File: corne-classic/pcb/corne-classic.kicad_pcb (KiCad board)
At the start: 2 copper layers, 133.8 x 92.2 mm, 98 parts, among them J1 MJ-4PP-9, J2 OLED, J3 LED, P1 i2c-pin, P2 i2c-pin, SW1 SW_PUSH, SW10 SW_PUSH, SW11 SW_PUSH, SW12 SW_PUSH, SW13 SW_PUSH, SW14 SW_PUSH, SW15 SW_PUSH, SW16 SW_PUSH, SW17 SW_PUSH, SW18 SW_PUSH, SW19 SW_PUSH, SW2 SW_PUSH, SW20 SW_PUSH, SW21 SW_PUSH, SW3 SW_PUSH, SW4 SW_PUSH, SW5 SW_PUSH, SW6 SW_PUSH, SW7 SW_PUSH, SW8 SW_PUSH, SW9 SW_PUSH, U1 ProMicro

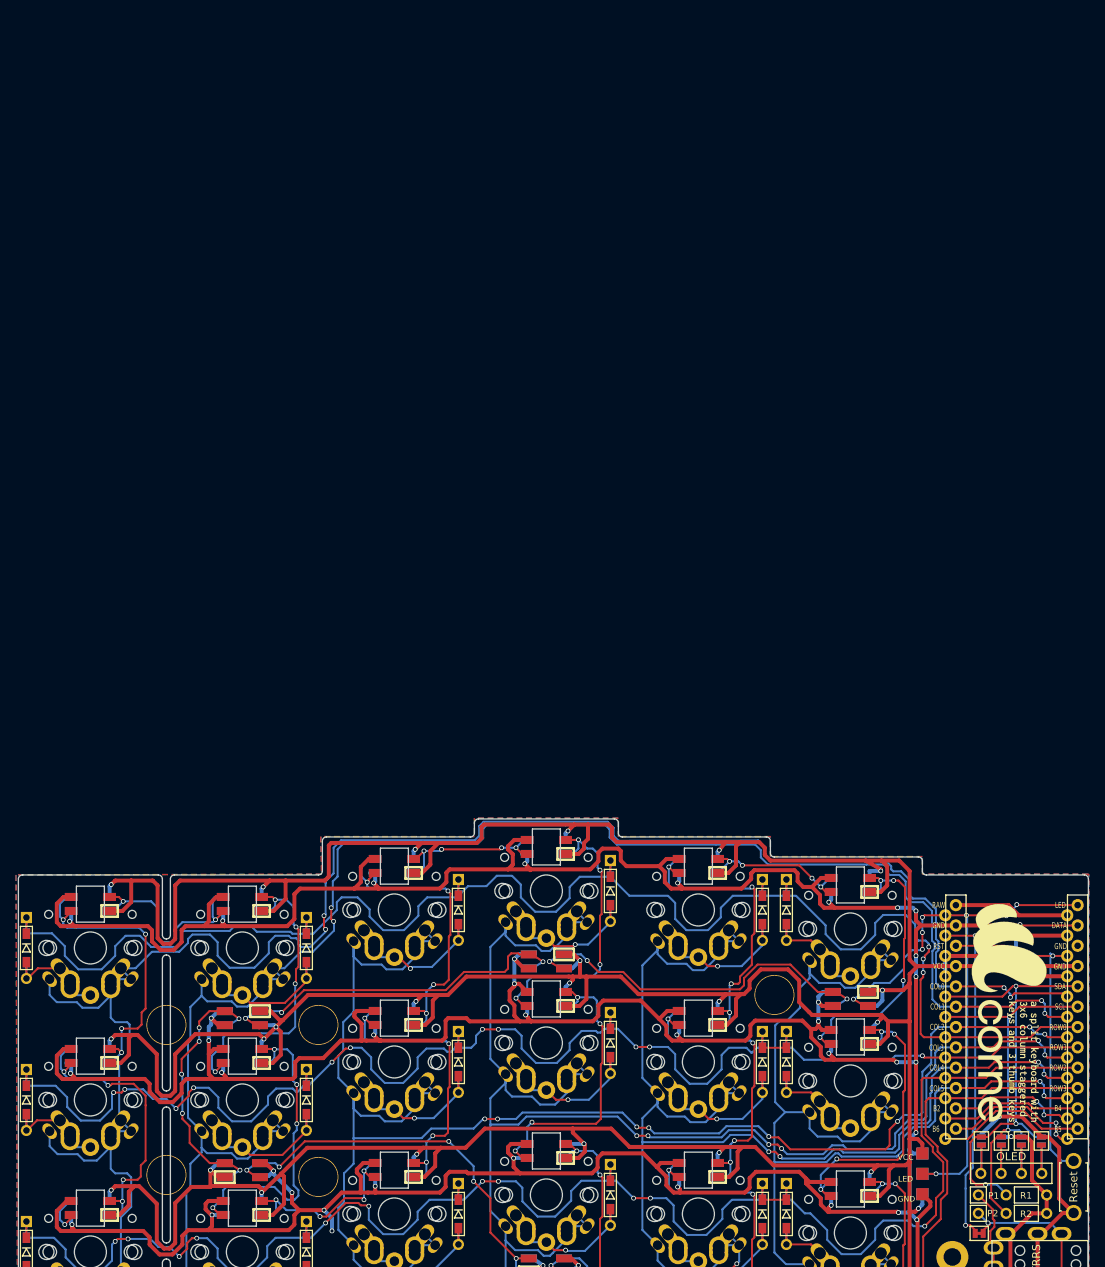
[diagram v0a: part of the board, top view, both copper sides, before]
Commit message: Adding one layer of keys
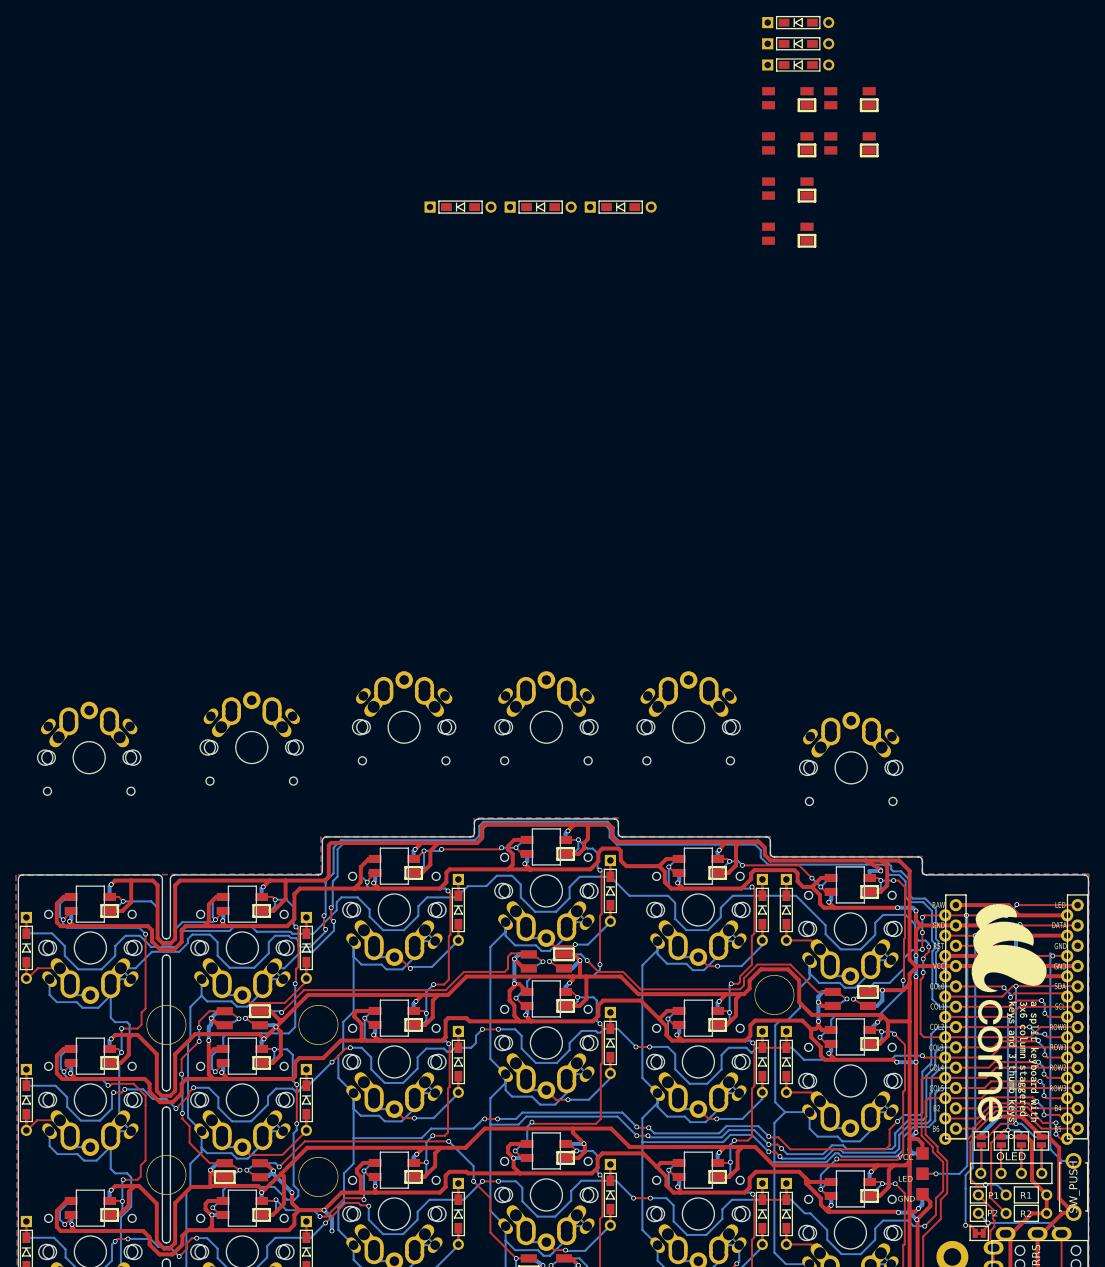
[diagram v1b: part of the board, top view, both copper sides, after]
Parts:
- added D22: D, kbd:D3_TH_SMD, F.Cu at (158.5, -33.2)
- added D23: D, kbd:D3_TH_SMD, F.Cu at (116.3, -15.5)
- added D24: D, kbd:D3_TH_SMD, F.Cu at (126.3, -15.5)
- added D25: D, kbd:D3_TH_SMD, F.Cu at (158.5, -38.5)
- added D26: D, kbd:D3_TH_SMD, F.Cu at (136.3, -15.5)
- added D27: D, kbd:D3_TH_SMD, F.Cu at (158.5, -35.9)
- added L28: SK6812MINI, kbd:SK6812MINI_rev, F.Cu at (157.2, -23.4)
- added L29: SK6812MINI, kbd:SK6812MINI_rev, F.Cu at (157.2, -29.1)
- added L30: SK6812MINI, kbd:SK6812MINI_rev, F.Cu at (164.9, -29.1)
- added L31: SK6812MINI, kbd:SK6812MINI_rev, F.Cu at (157.2, -12.1)
- added L32: SK6812MINI, kbd:SK6812MINI_rev, F.Cu at (157.2, -17.8)
- added L33: SK6812MINI, kbd:SK6812MINI_rev, F.Cu at (164.9, -23.4)
- added SW22: SW_PUSH, kbd:MX_ALPS_PG1350_noLed, F.Cu at (69.8, 53.3)
- added SW23: SW_PUSH, kbd:MX_ALPS_PG1350_noLed, F.Cu at (90.2, 52.1)
- added SW24: SW_PUSH, kbd:MX_ALPS_PG1350_noLed, F.Cu at (109.2, 49.5)
- added SW25: SW_PUSH, kbd:MX_ALPS_PG1350_noLed, F.Cu at (127.0, 49.5)
- added SW26: SW_PUSH, kbd:MX_ALPS_PG1350_noLed, F.Cu at (144.8, 49.5)
- added SW27: SW_PUSH, kbd:MX_ALPS_PG1350_noLed, F.Cu at (165.1, 54.6)
- RSW1: value Reset -> SW_PUSH
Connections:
- U1 pad 11: Net-(U1-Pad11) -> row4
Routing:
- net row4: track 0.00 -> 17.6 mm
- net Net-(U1-Pad11): track 17.6 -> 0.00 mm

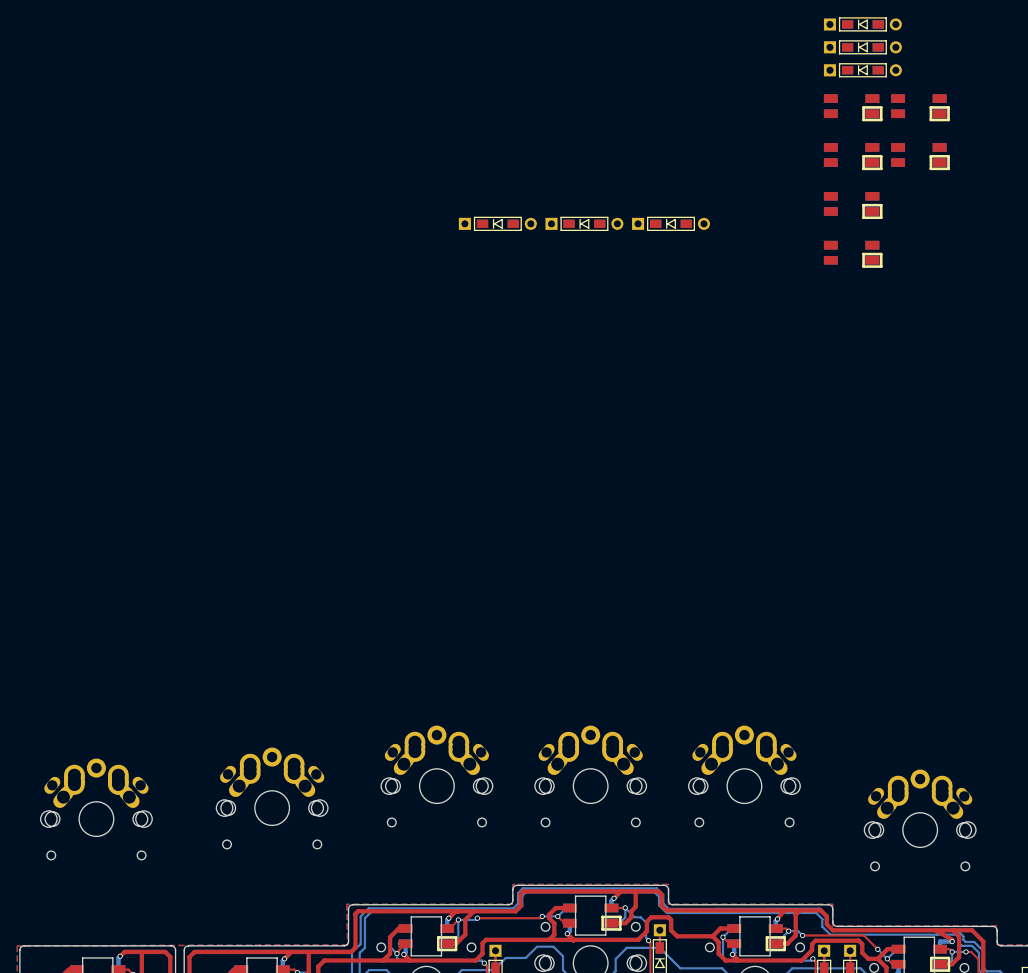
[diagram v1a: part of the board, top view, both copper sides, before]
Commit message: footprint placement
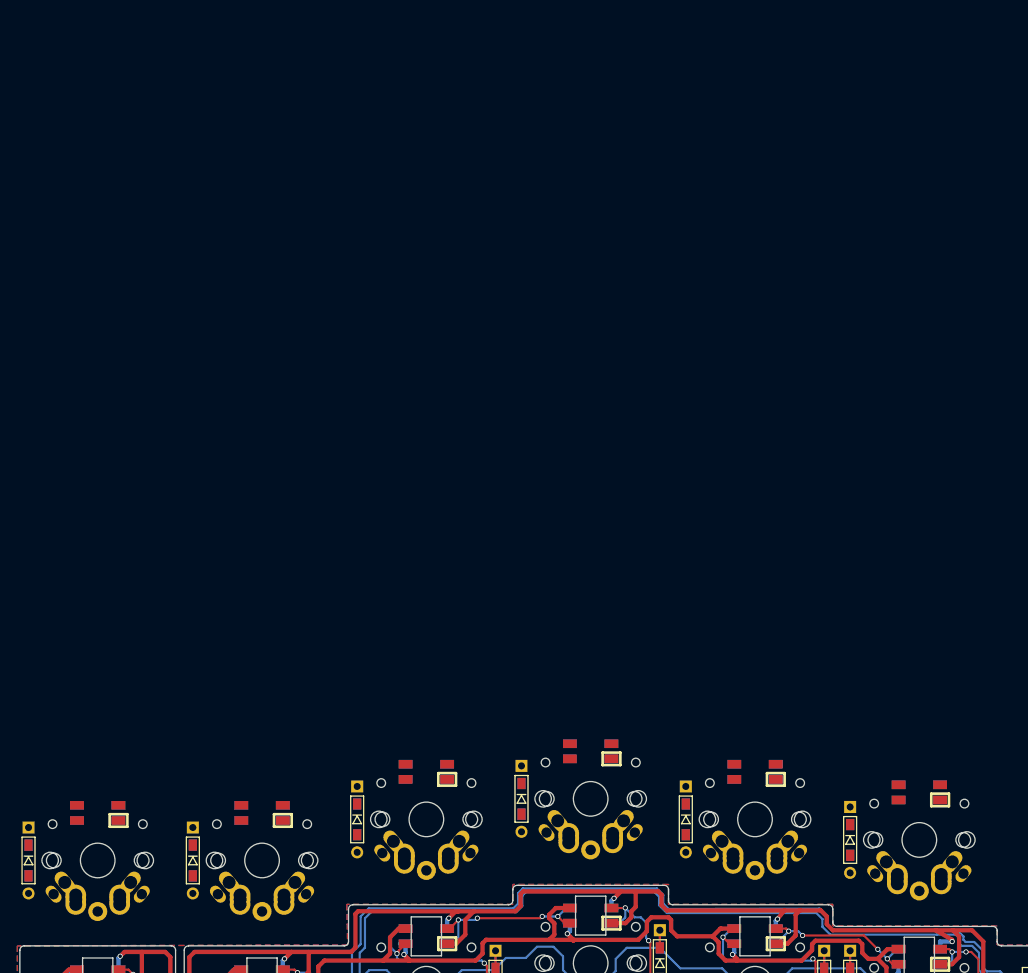
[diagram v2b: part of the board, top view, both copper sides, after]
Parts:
- moved D22 132.9 mm to (62.0, 58.1), turned to 270 degrees
- moved L28 115.7 mm to (70.0, 52.6)
- moved L29 106.4 mm to (89.0, 52.6)
- moved D25 97.9 mm to (119.0, 51.0), turned to 270 degrees
- moved L30 95.7 mm to (108.0, 47.9)
- moved D27 91.7 mm to (157.0, 55.8), turned to 270 degrees
- moved D23 81.6 mm to (81.0, 58.1), turned to 270 degrees
- moved D24 73.7 mm to (100.0, 53.4), turned to 270 degrees
- moved L33 73.7 mm to (165.0, 50.2)
- moved D26 68.9 mm to (138.0, 53.4), turned to 270 degrees
- moved L32 66.6 mm to (146.0, 47.9)
- moved L31 65.1 mm to (127.0, 45.5)
- moved SW23 6.17 mm to (89.0, 58.1), turned to 180 degrees
- moved SW22 4.79 mm to (70.0, 58.1), turned to 180 degrees
- moved SW24 4.03 mm to (108.0, 53.4), turned to 180 degrees
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
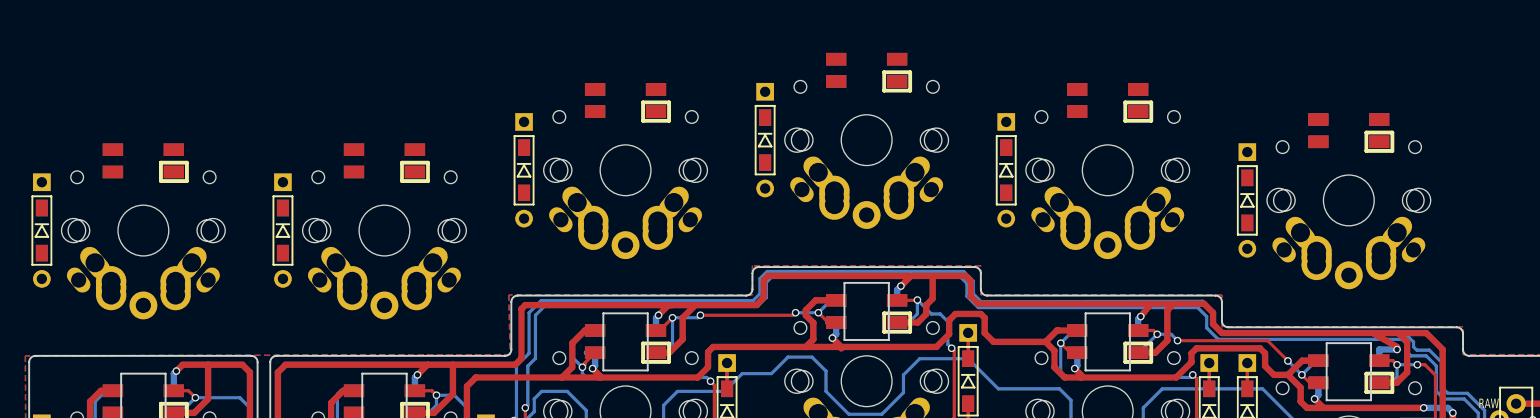
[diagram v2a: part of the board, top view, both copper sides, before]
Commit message: adding breakout board
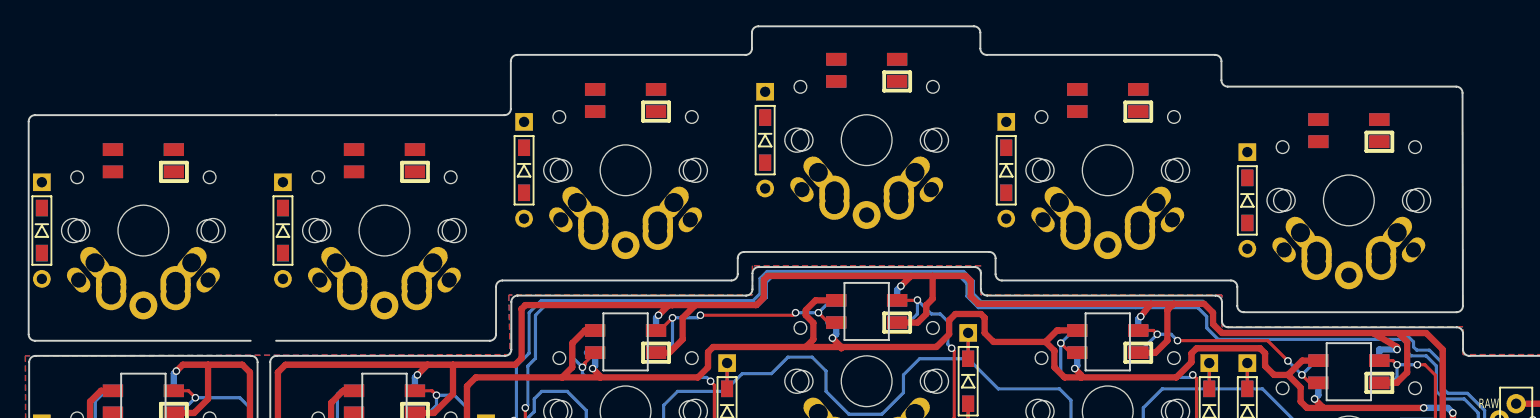
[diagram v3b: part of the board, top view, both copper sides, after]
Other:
- board size 133.8 x 92.2 mm -> 133.8 x 111.2 mm

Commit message: partial routing
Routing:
- net row4: track 17.6 -> 157.4 mm
- net VCC: track 759.0 -> 878.8 mm, vias 33 -> 37
- net GND: track 797.9 -> 911.2 mm, vias 49 -> 51
- net Net-(L30-Pad1): track 0.00 -> 51.0 mm
- net col5: track 187.0 -> 236.9 mm, vias 2 -> 3
- net col4: track 194.3 -> 242.8 mm, vias 6 -> 7
- net col3: track 225.1 -> 272.2 mm, vias 6 -> 10
- net Net-(L19-Pad1): track 5.40 -> 45.9 mm, vias 1 -> 5
- net col0: track 245.7 -> 283.9 mm, vias 4 -> 5
- net Net-(L31-Pad1): track 0.00 -> 28.8 mm, vias 0 -> 1
- net col2: track 197.5 -> 224.6 mm, vias 8 -> 9
- net Net-(L32-Pad1): track 0.00 -> 24.8 mm
- net col1: track 221.3 -> 236.7 mm
- net Net-(D24-Pad2): track 0.00 -> 14.6 mm
- net Net-(D26-Pad2): track 0.00 -> 14.6 mm
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- added copper zone on B.Cu, net (none)
- added copper zone on F.Cu, net (none)
- removed copper zone on B.Cu, net GND
- removed copper zone on F.Cu, net GND
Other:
- outline, holes or cut-outs redrawn

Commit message: routing done
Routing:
- net row4: track 157.4 -> 253.9 mm, vias 0 -> 4
- net GND: track 911.2 -> 990.9 mm, vias 51 -> 55
- net VCC: track 878.8 -> 956.0 mm, vias 37 -> 41
- net Net-(L29-Pad1): track 0.00 -> 53.7 mm, vias 0 -> 2
- net col3: track 272.2 -> 307.5 mm
- net Net-(L28-Pad1): track 3.52 -> 34.7 mm, vias 0 -> 3
- net Net-(L19-Pad1): track 45.9 -> 74.5 mm, vias 5 -> 8
- net col4: track 242.8 -> 268.8 mm
- net col2: track 224.6 -> 242.1 mm, vias 9 -> 10
- net Net-(L30-Pad1): track 51.0 -> 36.0 mm, vias 0 -> 3
- net col1: track 236.7 -> 250.7 mm, vias 4 -> 5
- net col5: track 236.9 -> 246.2 mm
- net Net-(L32-Pad1): track 24.8 -> 34.1 mm, vias 0 -> 3
- net Net-(L31-Pad1): track 28.8 -> 35.5 mm, vias 1 -> 3
- net Net-(L33-Pad1): track 0.00 -> 2.99 mm, vias 0 -> 1
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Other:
- outline, holes or cut-outs redrawn

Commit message: adding logo
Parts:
- removed the G*** at (184.0, 85.2)
- removed the G*** at (184.7, 85.3)
- added G***: LOGO, logo:korne_logo_smoll, B.Cu at (183.8, 84.3)
- added G***: LOGO, logo:korne_logo_smoll, F.Cu at (185.4, 84.2)
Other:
- board text added: "Korne Keyboard PCB by Gnu-Bricoleur Forked from foostan's Corne"
- board text removed: "Corne Classic v2.0 PCB designed by foostan"
